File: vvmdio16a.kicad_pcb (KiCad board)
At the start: 2 copper layers, 35 x 60 mm, 11 parts, among them J1 517-N2508-6002RB, J2 517-N2520-6002RB, SW1 220ADC16, U1 MCP23017

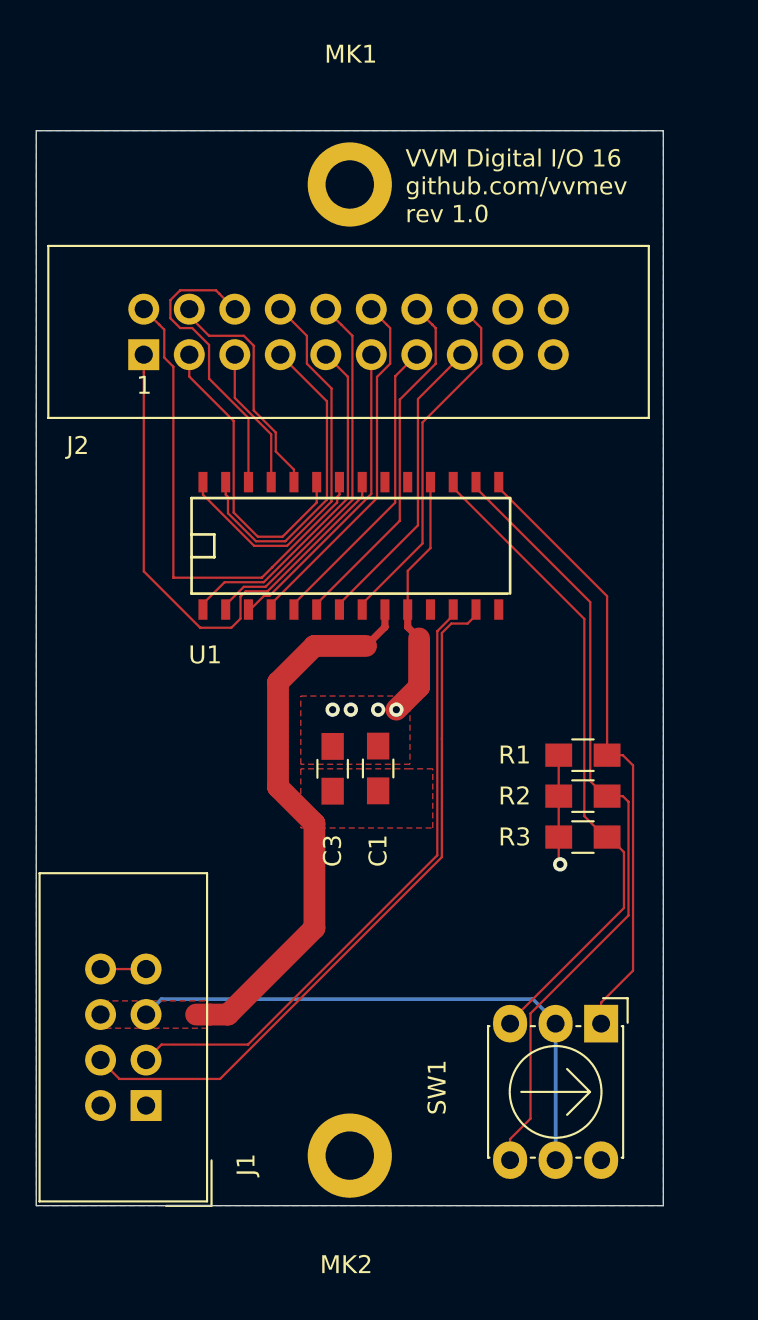
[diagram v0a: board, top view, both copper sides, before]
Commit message: Use correct footprint for IC
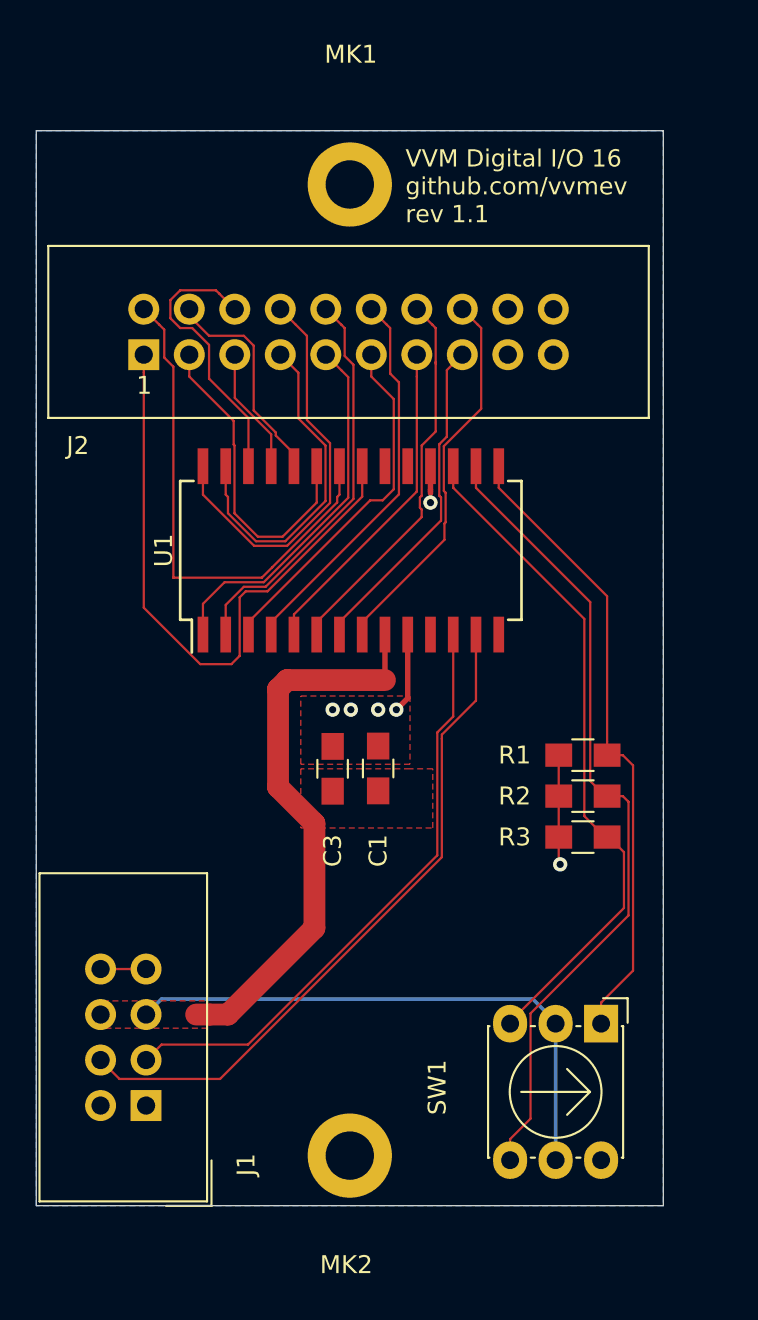
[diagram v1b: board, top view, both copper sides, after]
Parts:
- U1: footprint SMD_Packages:SOIC-28 -> Housings_SOIC:SOIC-28W_7.5x18.7mm_Pitch1.27mm
- moved U1 0.25 mm to (146.6, 90.4), turned to 90 degrees
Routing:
- net GND: track 20.1 -> 12.1 mm, vias 5 -> 6
- net /IO1: track 30.2 -> 34.2 mm
- net /IO11: track 17.4 -> 19.9 mm
- net /IO13: track 17.1 -> 19.2 mm
- net /SDA: track 39.8 -> 37.8 mm
- net /IO12: track 20.0 -> 21.8 mm
- net /IO14: track 20.0 -> 21.5 mm
- net /IO15: track 17.1 -> 18.5 mm
- net /IO16: track 20.0 -> 21.4 mm
- net /IO10: track 21.0 -> 22.5 mm
- net /IO9: track 19.4 -> 20.8 mm
- net /SCL: track 35.1 -> 33.7 mm
- net /IO7: track 18.1 -> 18.7 mm
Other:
- board text added: "VVM Digital I/O 16 github.com/vvmev rev 1.1"
- board text removed: "VVM Digital I/O 16 github.com/vvmev rev 1.0"
